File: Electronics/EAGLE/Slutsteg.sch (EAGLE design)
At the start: 167 parts, among them CN1 OSTYK33102030-2, CN2 OSTYK33102030-2, CN3 OSTYK33102030-2, IC1 SPX1117M3-L-3-3_TR, IC10 LM324D, IC11 L78M12ABDT-TR, IC2 L78M12ABDT-TR, IC3 ESP32-WROVER-IE-4MB, IC4 TM8211, IC5 LM324D, IC6 TPA3244DDWR, IC7 TPA3251D2DDVR, IC8 LM324D, IC9 LM324D, J1 0532610671, J2 JW-PJ-307-4H, J4 B4P-VH_LF__SN_, SW3 PDB181-K420F-103A2

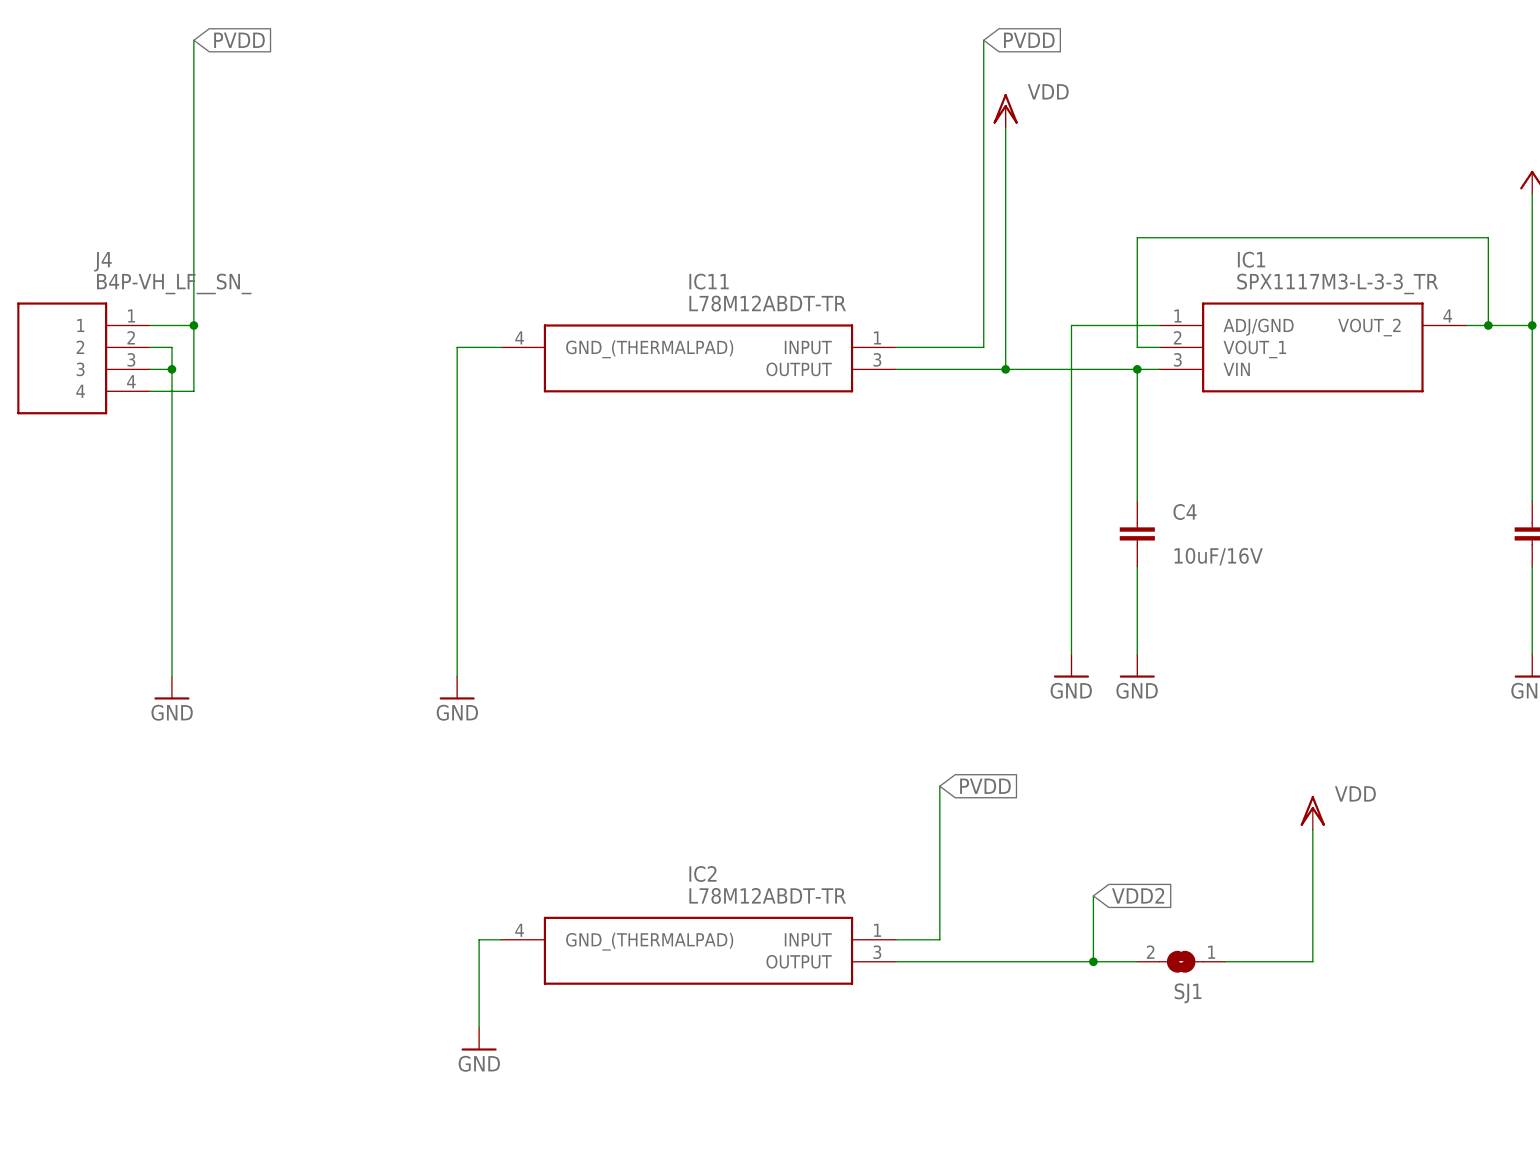
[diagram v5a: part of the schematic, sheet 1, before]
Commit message: Almost done with first draft of layout.
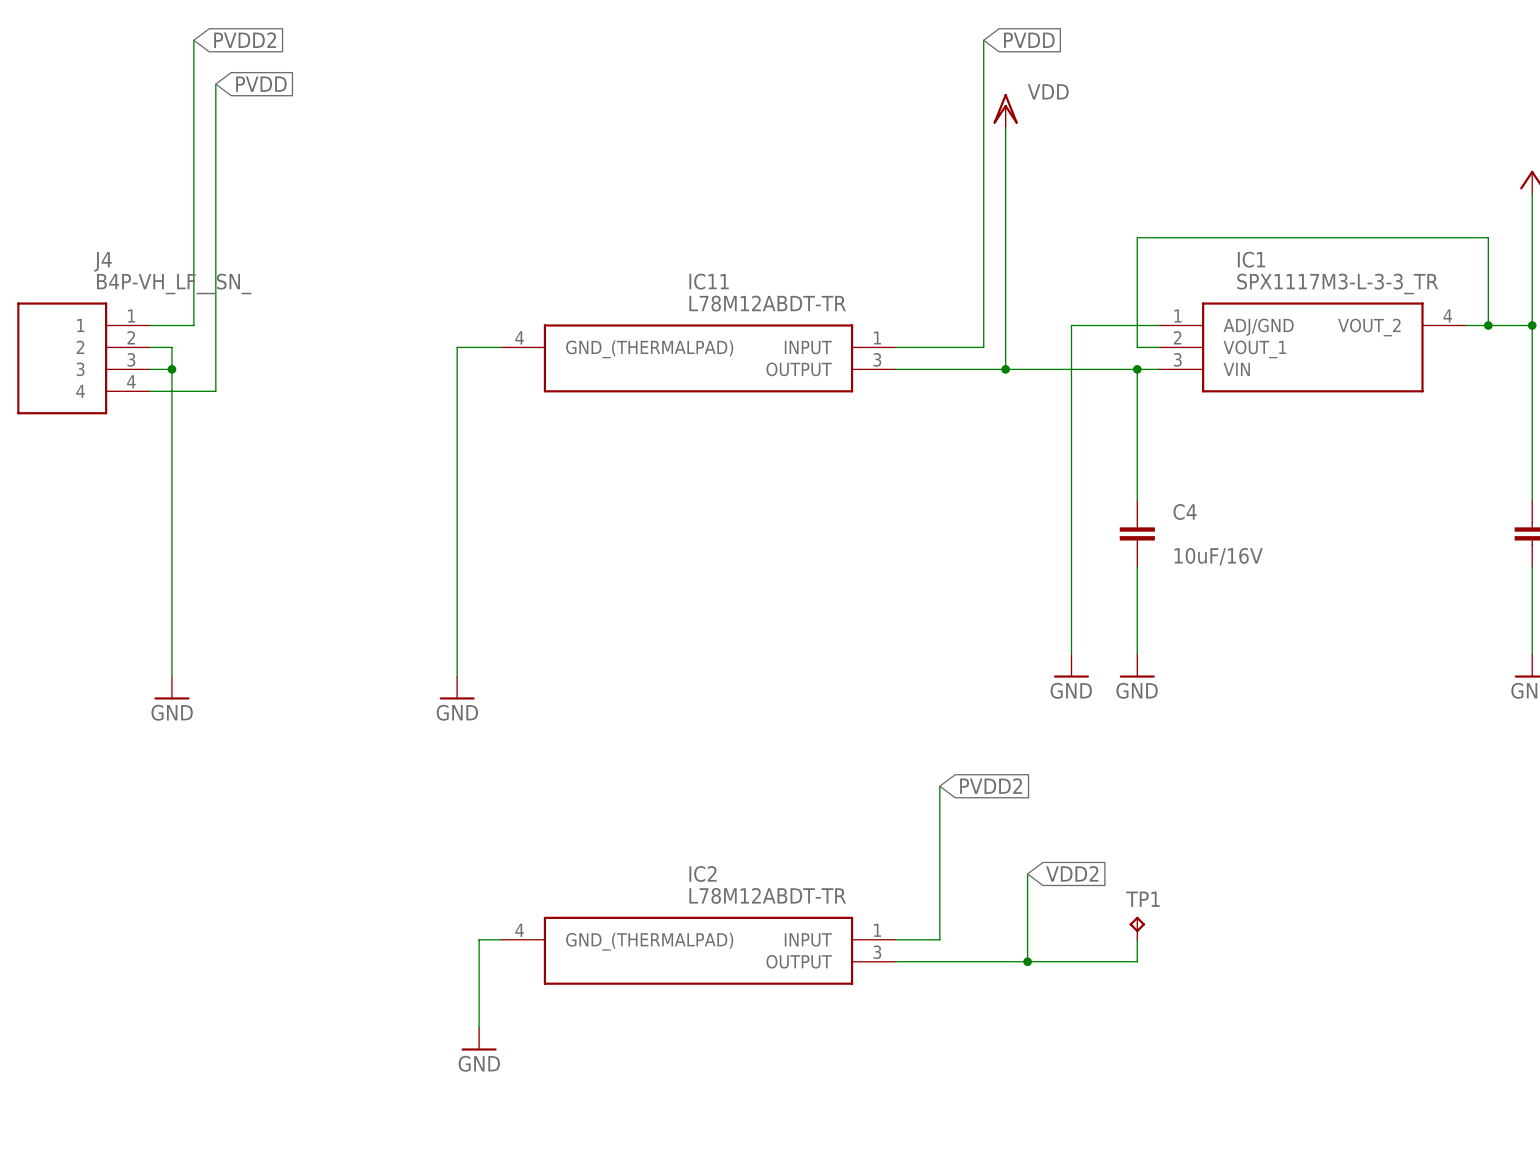
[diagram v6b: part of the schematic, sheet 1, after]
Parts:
- removed C76: 1uF/50V, rcl:C-EUC0805
- added C84: 100nF/50V, rcl:C-EUC0603
- added SJ2: (no value), jumper:SJ
- added TP1: TPB2,54, testpad:TPB2,54
- C24: value 1uF/50V -> 100nF/50V; device rcl:C-EUC0805 -> rcl:C-EUC0603
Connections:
- removed net BASE_OUT: IC10.OUTPUT_4, R49.2, SW3.2, SW3.3
- removed net BASE_OUT2: IC5.OUTPUT_1, R50.1
- removed net BLE-L: C14.1, IC10.INVERTING_INPUT_2, IC10.OUTPUT_2
- removed net BLE-R: C9.1, IC10.INVERTING_INPUT_1, IC10.OUTPUT_1
- removed net LEFT_OUT: IC8.OUTPUT_1, R46.5, R46.6, R52.1
- removed net LEFT_OUT2: IC5.OUTPUT_4, R51.2
- removed net RIGHT_OUT: IC8.OUTPUT_4, R46.2, R46.3, R54.1
- removed net RIGHT_OUT2: IC5.OUTPUT_3, R53.2
- new net GSDJT: C9.1, IC10.INVERTING_INPUT_1, IC10.OUTPUT_1, SJ1.1
- new net PVDD2: C56.1, C57.2, C59.2, C60.1, C63.+, C64.+, IC2.INPUT, IC7.PVDD_AB_1, IC7.PVDD_AB_2, IC7.PVDD_AB_3, IC7.PVDD_CD_1, IC7.PVDD_CD_2, IC7.PVDD_CD_3, J4.1
- new net TGHJESYRJK: C14.1, IC10.INVERTING_INPUT_2, IC10.OUTPUT_2, SJ2.1
- net GND: now also C84.2; no longer C76.2
- net INPUT_A: now also IC5.OUTPUT_3, R53.2
- net INPUT_A_SLAVE: now also IC5.OUTPUT_1, R50.1
- net INPUT_B: now also IC8.OUTPUT_4, R46.2, R46.3, R54.1
- net INPUT_B_SLAVE: now also IC10.OUTPUT_4, R49.2, SW3.2, SW3.3
- net INPUT_C: now also IC5.OUTPUT_4, R51.2
- net INPUT_D: now also IC8.OUTPUT_1, R46.5, R46.6, R52.1
- net N$6: now also C84.1; no longer C24.1
- net PVDD: no longer C56.1, C57.2, C59.2, C60.1, C63.+, C64.+, IC2.INPUT, IC7.PVDD_AB_1, IC7.PVDD_AB_2, IC7.PVDD_AB_3, IC7.PVDD_CD_1, IC7.PVDD_CD_2, IC7.PVDD_CD_3, J4.1
- net SIG_IN_LEFT: now also SJ2.2
- net SIG_IN_RIGHT: now also SJ1.2
- net VDD: now also C24.1; no longer C76.1, SJ1.1
- net VDD2: now also TP1.TP; no longer SJ1.2
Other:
- moved on the sheet: C24

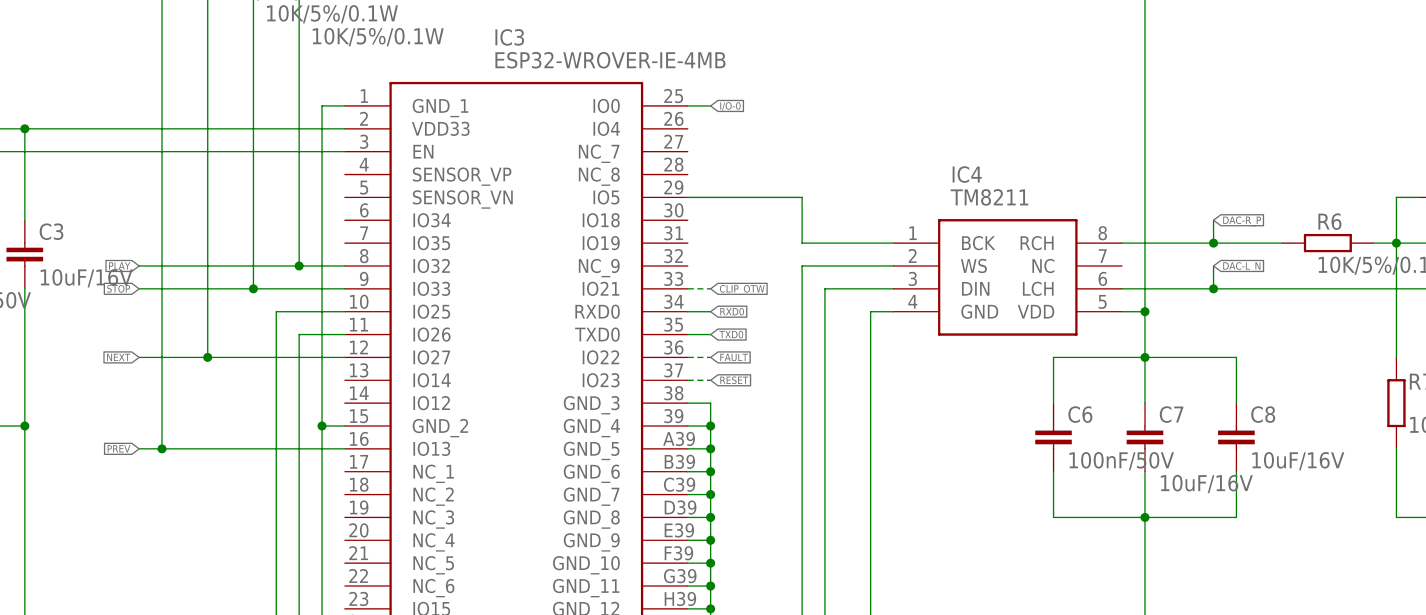
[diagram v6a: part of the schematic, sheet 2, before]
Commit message: Added some test points. More to come....
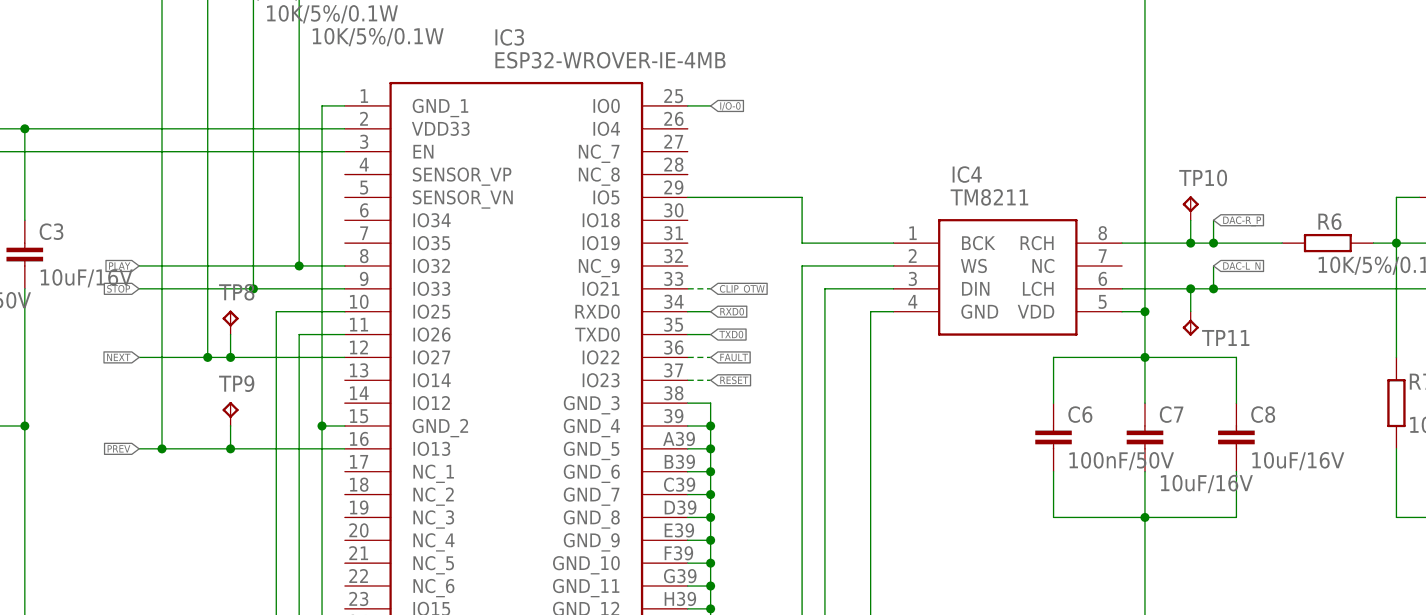
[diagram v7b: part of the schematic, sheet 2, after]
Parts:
- added TP10, TP11, TP2, TP3, TP4, TP5, TP8, TP9: TPB1,27, testpad:TPB1,27
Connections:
- net +3V3: now also TP4.TP
- net DAC-L_N: now also TP11.TP
- net DAC-R_P: now also TP10.TP
- net NEXT: now also TP8.TP
- net PREV: now also TP9.TP
- net PVDD: now also TP3.TP
- net PVDD2: now also TP2.TP
- net VDD: now also TP5.TP

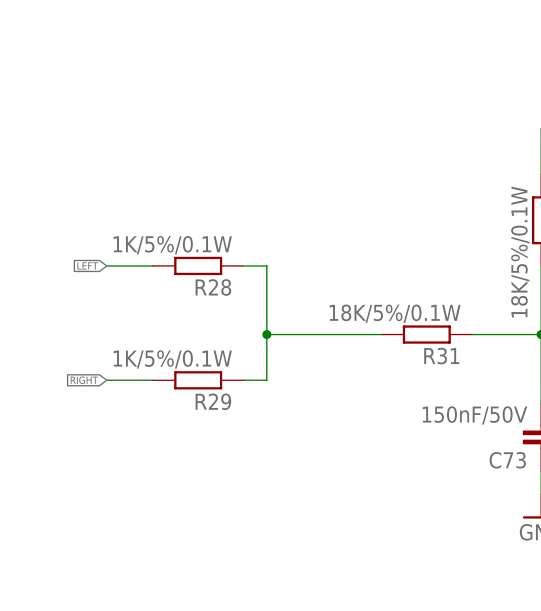
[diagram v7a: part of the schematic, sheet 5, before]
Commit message: TPs och Viastiching
TP,VIAstich,borrhål
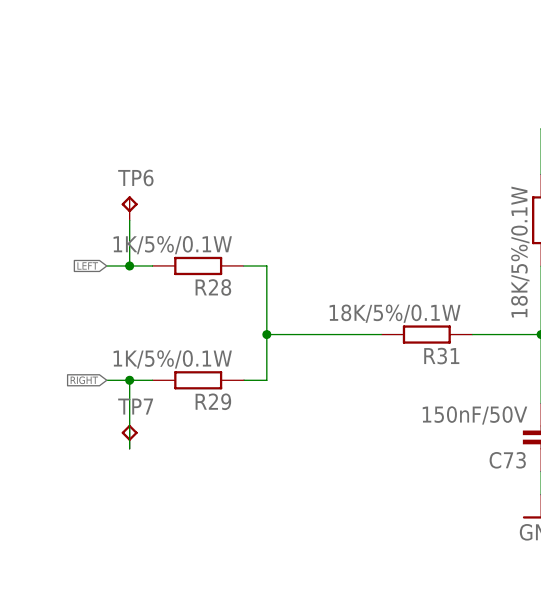
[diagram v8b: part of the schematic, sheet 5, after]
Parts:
- added TP6, TP7: TPB1,27, testpad:TPB1,27
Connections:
- net LEFT: now also TP6.TP
- net RIGHT: now also TP7.TP
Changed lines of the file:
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@@
 <part name="TP10" library="testpad" library_urn="urn:adsk.eagle:library:385" deviceset="TP" device="B1,27" package3d_urn="urn:adsk.eagle:package:27944/2" override_package3d_urn="urn:adsk.eagle:package:27379176/2" override_package_urn="urn:adsk.eagle:footprint:27900/1"/>
 <part name="TP11" library="testpad" library_urn="urn:adsk.eagle:library:385" deviceset="TP" device="B1,27" package3d_urn="urn:adsk.eagle:package:27944/2" override_package3d_urn="urn:adsk.eagle:package:27379176/2" override_package_urn="urn:adsk.eagle:footprint:27900/1"/>
+<part name="TP6" library="testpad" library_urn="urn:adsk.eagle:library:385" deviceset="TP" device="B1,27" package3d_urn="urn:adsk.eagle:package:27944/2"/>
+<part name="TP7" library="testpad" library_urn="urn:adsk.eagle:library:385" deviceset="TP" device="B1,27" package3d_urn="urn:adsk.eagle:package:27944/2"/>
 </parts>
 <sheets>
@@
 <attribute name="VALUE" x="204.6986" y="223.2406" size="2.0828" layer="96" ratio="6" rot="SMR90"/>
 </instance>
+<instance part="TP6" gate="G$1" x="48.26" y="83.82" smashed="yes">
+<attribute name="NAME" x="46.99" y="85.09" size="1.778" layer="95"/>
+<attribute name="TP_SIGNAL_NAME" x="49.53" y="82.55" size="1.778" layer="97"/>
+</instance>
+<instance part="TP7" gate="G$1" x="48.26" y="58.42" smashed="yes">
+<attribute name="NAME" x="46.99" y="59.69" size="1.778" layer="95"/>
+<attribute name="TP_SIGNAL_NAME" x="49.53" y="57.15" size="1.778" layer="97"/>
+</instance>
 </instances>
 <busses>
@@
 <segment>
 <pinref part="R29" gate="G$1" pin="2"/>
-<wire x1="50.8" y1="63.5" x2="45.72" y2="63.5" width="0.1524" layer="91"/>
+<wire x1="50.8" y1="63.5" x2="48.26" y2="63.5" width="0.1524" layer="91"/>
 <label x="45.72" y="63.5" size="0.8128" layer="95" rot="R180" xref="yes"/>
+<pinref part="TP7" gate="G$1" pin="TP"/>
+<wire x1="48.26" y1="63.5" x2="45.72" y2="63.5" width="0.1524" layer="91"/>
+<wire x1="48.26" y1="55.88" x2="48.26" y2="63.5" width="0.1524" layer="91"/>
+<junction x="48.26" y="63.5"/>
 </segment>
 <segment>
@@
 <segment>
 <pinref part="R28" gate="G$1" pin="2"/>
-<wire x1="50.8" y1="76.2" x2="45.72" y2="76.2" width="0.1524" layer="91"/>
+<wire x1="50.8" y1="76.2" x2="48.26" y2="76.2" width="0.1524" layer="91"/>
 <label x="45.72" y="76.2" size="0.8128" layer="95" rot="R180" xref="yes"/>
-</segment>
-<segment>
+<pinref part="TP6" gate="G$1" pin="TP"/>
+<wire x1="48.26" y1="76.2" x2="45.72" y2="76.2" width="0.1524" layer="91"/>
+<wire x1="48.26" y1="81.28" x2="48.26" y2="76.2" width="0.1524" layer="91"/>
+<junction x="48.26" y="76.2"/>
+</segment>
+<segment>
